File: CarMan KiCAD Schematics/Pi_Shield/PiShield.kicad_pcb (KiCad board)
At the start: 2 copper layers, 57.8 x 76.4 mm, 22 parts, among them J1 J1, J2 J2, J3 PICAN 2 Connector, J4 Motor Controller Header, J5 TSI Header, J6 PICAN 2 Connector, J7 CAN Testing Header, U1 RaspberryPi3, U10 BNO_055, U11 Raspberry_Pi_RTC

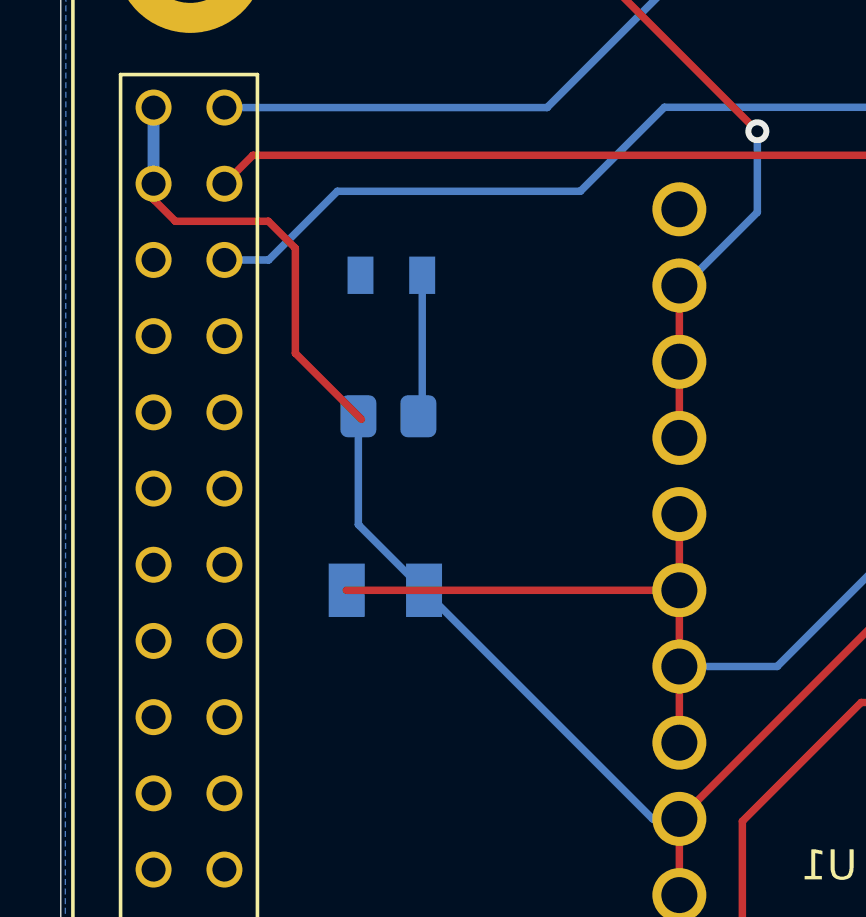
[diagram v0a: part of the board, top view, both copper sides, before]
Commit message: Added the README files and fixed the PCB layout line error
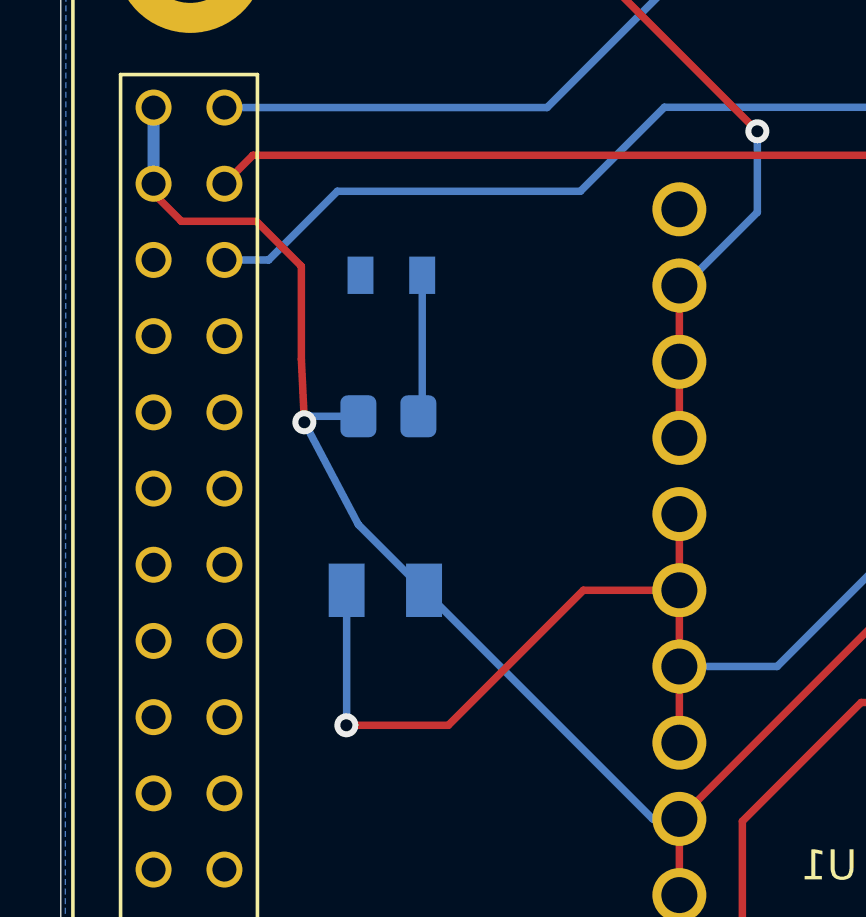
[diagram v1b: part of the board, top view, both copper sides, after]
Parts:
- D1: value LED -> D1
- D2: value LED -> D2
- D3: value LED -> D3
- J1: value J1 -> I2C Testing Header; footprint Connector_PinSocket_2.54mm:PinSocket_1x04_P2.54mm_Vertical -> Connector_PinHeader_2.54mm:PinHeader_1x04_P2.54mm_Vertical
- J3: value PICAN 2 Connector -> J3
- J4: value Motor Controller Header -> J4
- J5: value TSI Header -> J5
- J6: value PICAN 2 Connector -> J6
- J7: value CAN Testing Header -> J7
- PS1: value Regulator -> PS1
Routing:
- net Net-(C1-Pad1): track 74.8 -> 81.2 mm, vias 3 -> 4
- net /5V: track 82.2 -> 83.2 mm, vias 1 -> 2
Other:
- board text added: "Electrical & Computer Engineering Tafita Rakoto Pi Shield v. 1.0 Lafayette College"
- board text removed: "Electrical & Computer Engineering Tafita Rakoto Pi Shield v. 1.0"
